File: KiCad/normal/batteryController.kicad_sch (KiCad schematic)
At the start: 10 parts, among them J1 Conn_02x08_Counter_Clockwise, J2 Screw_Terminal_01x02, J3 USB_A, U1 ATtiny45V-10P, U2 L7806CV, U3 L78L05_SOT89

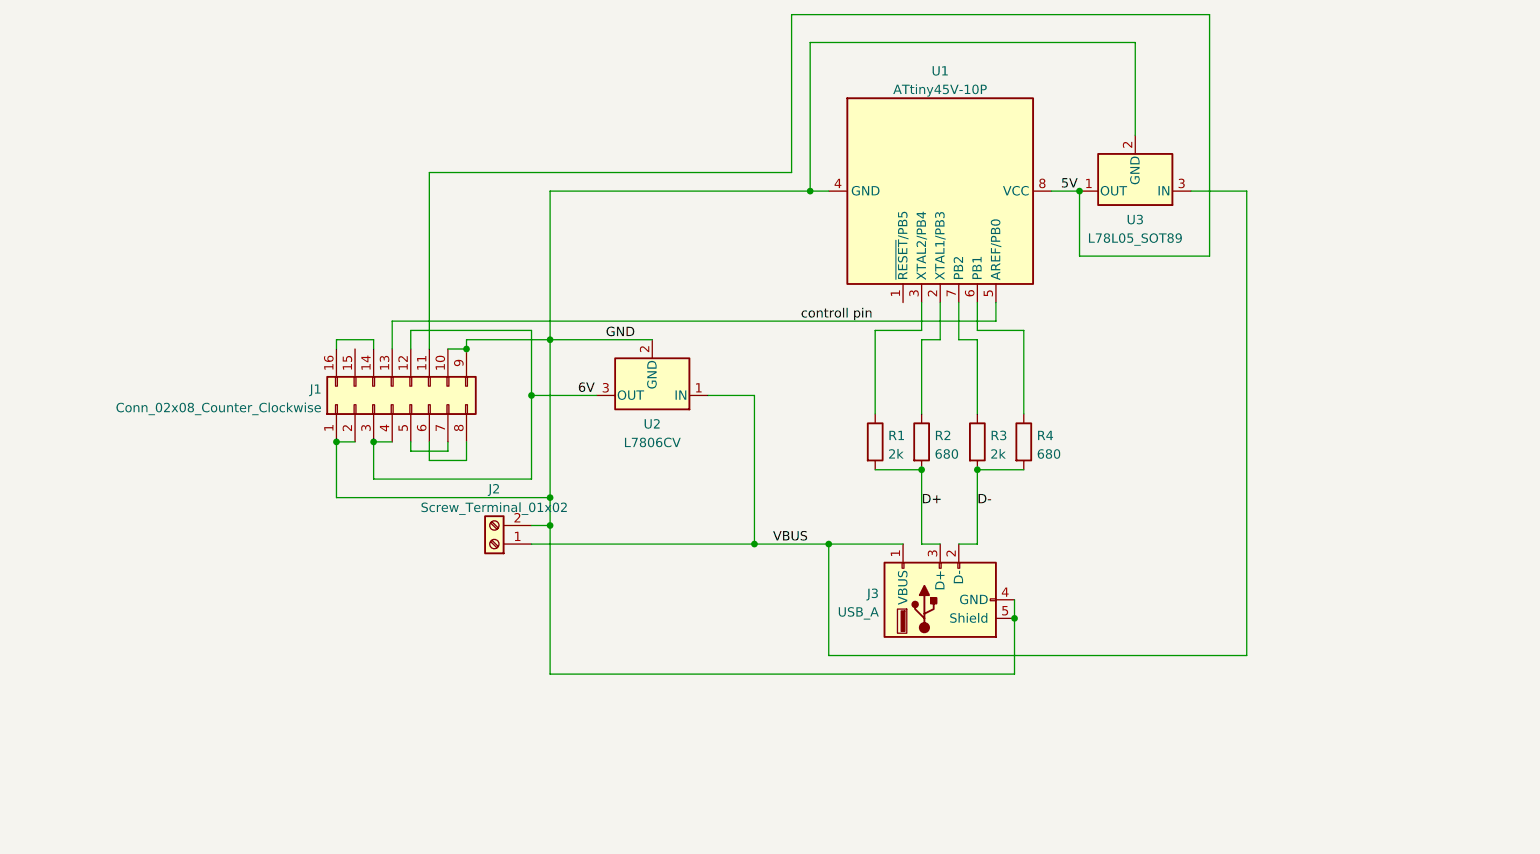
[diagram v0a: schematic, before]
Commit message: redesign to use switching voltage regulator
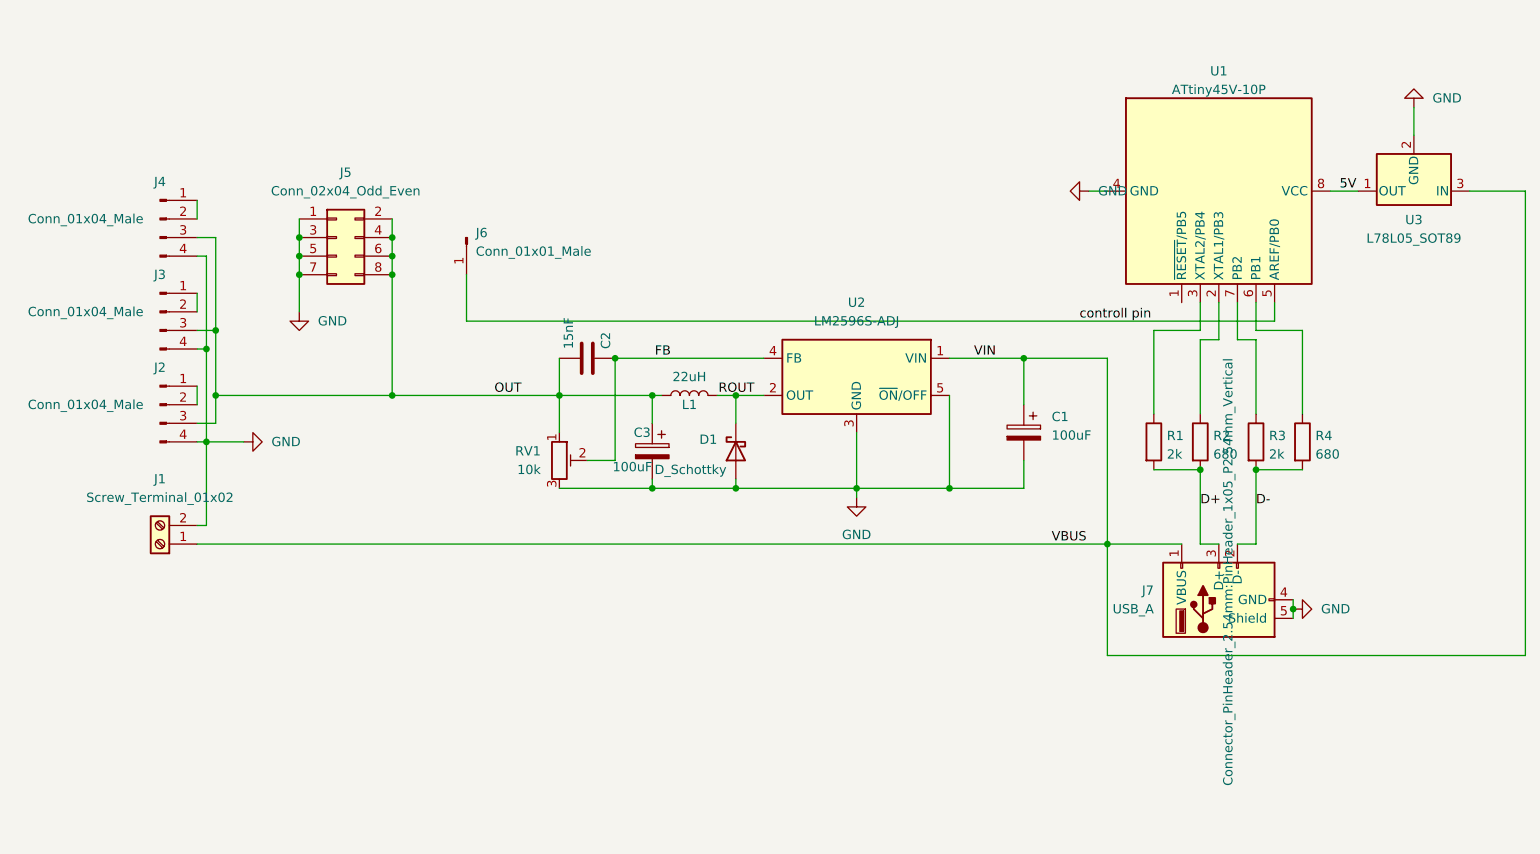
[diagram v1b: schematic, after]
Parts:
- removed J1: Conn_02x08_Counter_Clockwise, Connector_PinHeader_2.54mm:PinHeader_2x08_P2.54mm_Vertical, symbol Connector_Generic:Conn_02x08_Counter_Clockwise
- removed U2: L7806CV, Package_TO_SOT_THT:TO-220-3_Horizontal_TabDown, symbol Regulator_Linear:L7806
- added C1, C3: 100uF, Capacitor_THT:CP_Radial_D6.3mm_P2.50mm, symbol Device:C_Polarized
- added C2: 15nF, Capacitor_THT:C_Rect_L7.0mm_W2.5mm_P5.00mm, symbol Device:C
- added D1: D_Schottky, Diode_THT:D_DO-41_SOD81_P7.62mm_Horizontal, symbol Device:D_Schottky
- added J2, J3, J4: Conn_01x04_Male, Connector_PinHeader_2.54mm:PinHeader_1x04_P2.54mm_Vertical, symbol Connector:Conn_01x04_Male
- added J5: Conn_02x04_Odd_Even, Connector_PinHeader_2.54mm:PinHeader_2x04_P2.54mm_Vertical, symbol Connector_Generic:Conn_02x04_Odd_Even
- added J6: Conn_01x01_Male, Connector_PinHeader_2.54mm:PinHeader_1x01_P2.54mm_Vertical, symbol Connector:Conn_01x01_Male
- added L1: 22uH, custom:sdr1006, symbol Device:L
- added RV1: 10k, Potentiometer_THT:Potentiometer_Bourns_3266Y_Vertical, symbol Device:R_Potentiometer_Trim
- added U2: LM2596S-ADJ, Package_TO_SOT_SMD:TO-263-5_TabPin3, symbol Regulator_Switching:LM2596S-ADJ
- J1: renamed from J2; footprint TerminalBlock:TerminalBlock_bornier-2_P5.08mm -> TerminalBlock_Phoenix:TerminalBlock_Phoenix_MPT-0,5-2-2.54_1x02_P2.54mm_Horizontal
- J7: renamed from J3; footprint Connector_USB:USB_A_CNCTech_1001-011-01101_Horizontal -> Connector_PinHeader_2.54mm:PinHeader_1x05_P2.54mm_Vertical
- R1, R2, R3, R4: footprint Resistor_SMD:R_0402_1005Metric -> Resistor_THT:R_Axial_DIN0207_L6.3mm_D2.5mm_P7.62mm_Horizontal
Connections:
- net GND: now also C1.2, C3.2, D1.2 (A), J2.4 (Pin_4), J3.4 (Pin_4), J4.4 (Pin_4), J5.1 (Pin_1), J5.3 (Pin_3), J5.5 (Pin_5), J5.7 (Pin_7), RV1.3, U2.3 (GND), U2.5 (~{ON}/OFF)
- net VBUS: now also C1.1, U2.1 (VIN)
- net controll pin: now also J6.1 (Pin_1)
- new net: J2.1 (Pin_1), J2.2 (Pin_2)
- new net: J4.1 (Pin_1), J4.2 (Pin_2)
- new net: J3.1 (Pin_1), J3.2 (Pin_2)
- new net FB: C2.1, RV1.2, U2.4 (FB)
- new net OUT: C2.2, C3.1, J2.3 (Pin_3), J3.3 (Pin_3), J4.3 (Pin_3), J5.2 (Pin_2), J5.4 (Pin_4), J5.6 (Pin_6), J5.8 (Pin_8), L1.2, RV1.1
- new net ROUT: D1.1 (K), L1.1, U2.2 (OUT)
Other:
- moved on the sheet: J1, J7, R1, R2, R3, R4, U1, U3

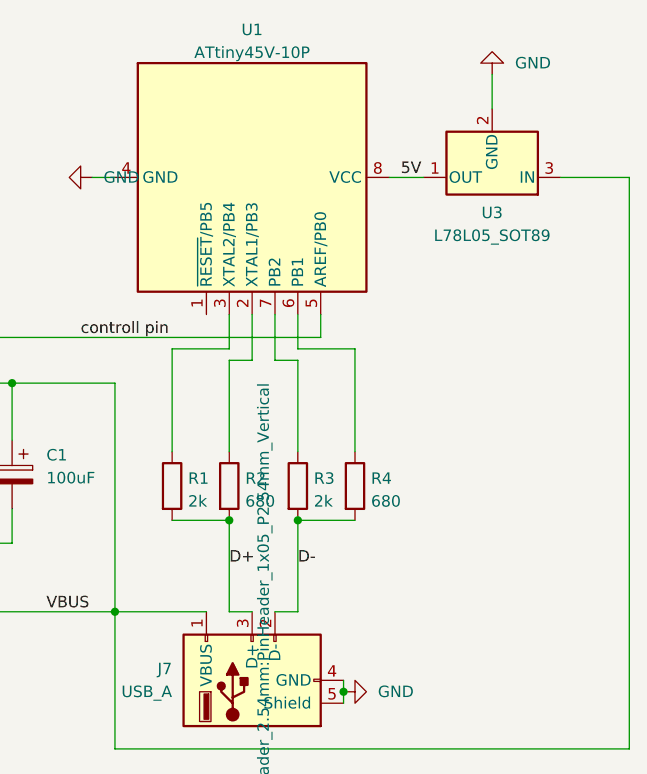
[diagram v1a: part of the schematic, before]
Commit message: changed 5v regulator
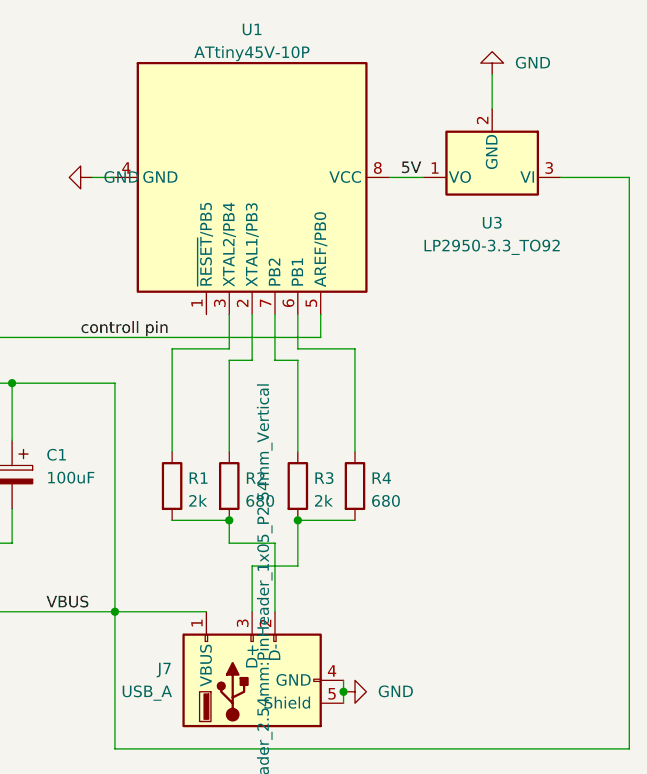
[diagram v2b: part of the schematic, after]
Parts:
- removed U3: L78L05_SOT89, Package_TO_SOT_SMD:SOT-89-3, symbol Regulator_Linear:L78L05_SOT89
- added U3: LP2950-3.3_TO92, Package_TO_SOT_THT:TO-92_Inline, symbol Regulator_Linear:LP2950-3.3_TO92
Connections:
- net 5V: now also U3.1 (VO)
- net GND: now also U3.2 (GND)
- net VBUS: now also U3.3 (VI)
- net D+: no longer names the net of R1.2, R2.2
- net D+: now also J7.2 (D-); no longer J7.3 (D+)
- net D-: no longer names the net of R3.2, R4.2
- net D-: now also J7.3 (D+); no longer J7.2 (D-)
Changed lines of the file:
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@@
   (junction (at 152.4 106.68) (diameter 0) (color 0 0 0 0)
   )
+  (junction (at 111.76 93.98) (diameter 0) (color 0 0 0 0)
+  )
+  (junction (at 76.2 74.93) (diameter 0) (color 0 0 0 0)
+  )
+  (junction (at 162.56 88.9) (diameter 0) (color 0 0 0 0)
+  )
+  (junction (at 76.2 93.98) (diameter 0) (color 0 0 0 0)
+  )
+  (junction (at 50.8 100.33) (diameter 0) (color 0 0 0 0)
+  )
+  (junction (at 99.06 93.98) (diameter 0) (color 0 0 0 0)
+  )
+  (junction (at 52.07 85.09) (diameter 0) (color 0 0 0 0)
+  )
+  (junction (at 76.2 77.47) (diameter 0) (color 0 0 0 0)
+  )
+  (junction (at 63.5 72.39) (diameter 0) (color 0 0 0 0)
+  )
+  (junction (at 123.19 93.98) (diameter 0) (color 0 0 0 0)
+  )
+  (junction (at 50.8 87.63) (diameter 0) (color 0 0 0 0)
+  )
+  (junction (at 111.76 106.68) (diameter 0) (color 0 0 0 0)
+  )
+  (junction (at 123.19 106.68) (diameter 0) (color 0 0 0 0)
+  )
+  (junction (at 52.07 93.98) (diameter 0) (color 0 0 0 0)
+  )
   (junction (at 186.69 104.14) (diameter 0) (color 0 0 0 0)
   )
-  (junction (at 111.76 93.98) (diameter 0) (color 0 0 0 0)
-  )
-  (junction (at 76.2 74.93) (diameter 0) (color 0 0 0 0)
-  )
-  (junction (at 162.56 88.9) (diameter 0) (color 0 0 0 0)
-  )
-  (junction (at 76.2 93.98) (diameter 0) (color 0 0 0 0)
-  )
-  (junction (at 50.8 100.33) (diameter 0) (color 0 0 0 0)
-  )
-  (junction (at 99.06 93.98) (diameter 0) (color 0 0 0 0)
-  )
-  (junction (at 52.07 85.09) (diameter 0) (color 0 0 0 0)
-  )
-  (junction (at 76.2 77.47) (diameter 0) (color 0 0 0 0)
-  )
-  (junction (at 63.5 72.39) (diameter 0) (color 0 0 0 0)
-  )
-  (junction (at 123.19 93.98) (diameter 0) (color 0 0 0 0)
-  )
-  (junction (at 50.8 87.63) (diameter 0) (color 0 0 0 0)
-  )
-  (junction (at 111.76 106.68) (diameter 0) (color 0 0 0 0)
-  )
-  (junction (at 123.19 106.68) (diameter 0) (color 0 0 0 0)
-  )
-  (junction (at 52.07 93.98) (diameter 0) (color 0 0 0 0)
-  )
   (junction (at 106.68 88.9) (diameter 0) (color 0 0 0 0)
   )
   (junction (at 63.5 74.93) (diameter 0) (color 0 0 0 0)
   )
+  (junction (at 194.31 104.14) (diameter 0) (color 0 0 0 0)
+  )
   (junction (at 76.2 72.39) (diameter 0) (color 0 0 0 0)
   )
@@
   (junction (at 139.7 106.68) (diameter 0) (color 0 0 0 0)
   )
-  (junction (at 194.31 104.14) (diameter 0) (color 0 0 0 0)
-  )
   (wire (pts (xy 215.9 54.61) (xy 215.9 58.42))
     (stroke (width 0) (type default) (color 0 0 0 0))
@@
     (stroke (width 0) (type default) (color 0 0 0 0))
   )
-  (wire (pts (xy 189.23 114.3) (xy 186.69 114.3))
-    (stroke (width 0) (type default) (color 0 0 0 0))
-  )
-  (wire (pts (xy 186.69 114.3) (xy 186.69 104.14))
-    (stroke (width 0) (type default) (color 0 0 0 0))
-  )
   (wire (pts (xy 106.68 88.9) (xy 127 88.9))
     (stroke (width 0) (type default) (color 0 0 0 0))
@@
     (stroke (width 0) (type default) (color 0 0 0 0))
   )
+  (wire (pts (xy 194.31 109.22) (xy 189.23 109.22))
+    (stroke (width 0) (type default) (color 0 0 0 0))
+  )
   (wire (pts (xy 106.68 102.87) (xy 102.87 102.87))
     (stroke (width 0) (type default) (color 0 0 0 0))
@@
     (stroke (width 0) (type default) (color 0 0 0 0))
   )
+  (wire (pts (xy 194.31 104.14) (xy 194.31 109.22))
+    (stroke (width 0) (type default) (color 0 0 0 0))
+  )
   (wire (pts (xy 200.66 85.09) (xy 200.66 96.52))
     (stroke (width 0) (type default) (color 0 0 0 0))
@@
     (stroke (width 0) (type default) (color 0 0 0 0))
   )
-  (wire (pts (xy 191.77 114.3) (xy 194.31 114.3))
-    (stroke (width 0) (type default) (color 0 0 0 0))
-  )
   (wire (pts (xy 63.5 72.39) (xy 63.5 74.93))
     (stroke (width 0) (type default) (color 0 0 0 0))
@@
     (stroke (width 0) (type default) (color 0 0 0 0))
   )
+  (wire (pts (xy 186.69 104.14) (xy 186.69 106.68))
+    (stroke (width 0) (type default) (color 0 0 0 0))
+  )
   (wire (pts (xy 162.56 95.25) (xy 162.56 88.9))
     (stroke (width 0) (type default) (color 0 0 0 0))
@@
     (stroke (width 0) (type default) (color 0 0 0 0))
   )
+  (wire (pts (xy 191.77 106.68) (xy 191.77 114.3))
+    (stroke (width 0) (type default) (color 0 0 0 0))
+  )
   (wire (pts (xy 123.19 93.98) (xy 120.65 93.98))
     (stroke (width 0) (type default) (color 0 0 0 0))
@@
     (stroke (width 0) (type default) (color 0 0 0 0))
   )
+  (wire (pts (xy 189.23 109.22) (xy 189.23 114.3))
+    (stroke (width 0) (type default) (color 0 0 0 0))
+  )
   (wire (pts (xy 173.99 129.54) (xy 231.14 129.54))
     (stroke (width 0) (type default) (color 0 0 0 0))
   )
+  (wire (pts (xy 186.69 106.68) (xy 191.77 106.68))
+    (stroke (width 0) (type default) (color 0 0 0 0))
+  )
   (wire (pts (xy 49.53 80.01) (xy 49.53 82.55))
     (stroke (width 0) (type default) (color 0 0 0 0))
@@
   )
   (wire (pts (xy 162.56 88.9) (xy 152.4 88.9))
-    (stroke (width 0) (type default) (color 0 0 0 0))
-  )
-  (wire (pts (xy 194.31 114.3) (xy 194.31 104.14))
     (stroke (width 0) (type default) (color 0 0 0 0))
   )
@@
   )
   (label "5V" (at 205.74 66.04 0)
-    (effects (font (size 1.27 1.27)) (justify left bottom))
-  )
-  (label "D+" (at 186.69 109.22 0)
-    (effects (font (size 1.27 1.27)) (justify left bottom))
-  )
-  (label "D-" (at 194.31 109.22 0)
     (effects (font (size 1.27 1.27)) (justify left bottom))
   )
@@
     (pin "8")
   )
+  (symbol (lib_id "Regulator_Linear:LP2950-3.3_TO92") (at 215.9 66.04 180) (unit 1)
+    (in_bom yes) (on_board yes) (fields_autoplaced)
+    (property "Reference" "U3" (id 0) (at 215.9 71.12 0))
+    (property "Value" "LP2950-3.3_TO92" (id 1) (at 215.9 73.66 0))
+    (property "Footprint" "Package_TO_SOT_THT:TO-92_Inline" (id 2) (at 215.9 71.755 0)
+      (effects (font (size 1.27 1.27) italic) hide)
+    )
+    (property "Datasheet" "http://www.ti.com/lit/ds/symlink/lp2950.pdf" (id 3) (at 215.9 64.77 0)
+      (effects (font (size 1.27 1.27)) hide)
+    )
+    (pin "1")
+    (pin "2")
+    (pin "3")
+  )
   (symbol (lib_id "Device:C_Polarized") (at 111.76 101.6 0) (mirror y) (unit 1)
     (in_bom yes) (on_board yes)
@@
     (pin "1")
     (pin "2")
-  )
-  (symbol (lib_id "Regulator_Linear:L78L05_SOT89") (at 215.9 66.04 180) (unit 1)
-    (in_bom yes) (on_board yes) (fields_autoplaced)
-    (property "Reference" "U3" (id 0) (at 215.9 69.9754 0))
-    (property "Value" "L78L05_SOT89" (id 1) (at 215.9 72.5123 0))
-    (property "Footprint" "Package_TO_SOT_SMD:SOT-89-3" (id 2) (at 215.9 71.12 0)
-      (effects (font (size 1.27 1.27) italic) hide)
-    )
-    (property "Datasheet" "http://www.st.com/content/ccc/resource/technical/document/datasheet/15/55/e5/aa/23/5b/43/fd/CD00000446.pdf/files/CD00000446.pdf/jcr:content/translations/en.CD00000446.pdf" (id 3) (at 215.9 64.77 0)
-      (effects (font (size 1.27 1.27)) hide)
-    )
-    (pin "1")
-    (pin "2")
-    (pin "3")
   )
   (symbol (lib_id "Device:R") (at 200.66 100.33 0) (unit 1)
@@
       (reference "U2") (unit 1) (value "LM2596S-ADJ") (footprint "Package_TO_SOT_SMD:TO-263-5_TabPin3")
     )
-    (path "/098683c7-693b-4459-b336-ef4e310c870b"
-      (reference "U3") (unit 1) (value "L78L05_SOT89") (footprint "Package_TO_SOT_SMD:SOT-89-3")
-    )
-  )
+    (path "/0630a5b9-6e05-4f50-8a4d-d803ec7f325f"
+      (reference "U3") (unit 1) (value "LP2950-3.3_TO92") (footprint "Package_TO_SOT_THT:TO-92_Inline")
+    )
+  )
